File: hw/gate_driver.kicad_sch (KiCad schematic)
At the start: 15 parts, among them IC501 LMG1210RVRT

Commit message: v0.3.0rc (v1.0.0rc) sch complete
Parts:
- removed D501: 0.62V, footprints:stm_STPS1170AF, symbol Device:D_Schottky
- removed IC501: LMG1210RVRT, footprints:ti_LMG1210RVRT, symbol ti_LMG1210RVRT:LMG1210RVRT
- removed TP19: GND, TestPoint:TestPoint_Pad_1.0x1.0mm, symbol Connector:TestPoint
- removed TP8: 5V, TestPoint:TestPoint_Pad_1.0x1.0mm, symbol Connector:TestPoint
- added C503: 100n, Resistor_SMD:R_0402_1005Metric, symbol Device:C_Small
- added C504: 470n, Resistor_SMD:R_0402_1005Metric, symbol Device:C_Small
- added D501, D502: GRN, LED_SMD:LED_0402_1005Metric, symbol Device:LED_Small
- added D503, D504, D505: 0.55, footprints:stm_STPS1170AF, symbol Device:D_Schottky_Small
- added D506, D507: 5.1, Diode_SMD:D_SOD-123, symbol Device:D_Zener_Small
- added Q501: BSS127S, Package_TO_SOT_SMD:SOT-23, symbol Transistor_FET:BSS127S
- added R505, R506, R507, R508: 0, Resistor_SMD:R_0402_1005Metric, symbol Device:R_Small
- added R509: 1.5, Resistor_SMD:R_0402_1005Metric, symbol Device:R_Small
- added SB501, SB502: Jumper, Jumper:SolderJumper-2_P1.3mm_Open_TrianglePad1.0x1.5mm, symbol Jumper:SolderJumper_2_Bridged
- added TP502: SWH+, TestPoint:TestPoint_Keystone_5000-5004_Miniature, symbol Connector:TestPoint
- added TP506: SWLO, TestPoint:TestPoint_Keystone_5000-5004_Miniature, symbol Connector:TestPoint
- added TP507: GND, TestPoint:TestPoint_Keystone_5000-5004_Miniature, symbol Connector:TestPoint
- added TP508: PWM_CONV, TestPoint:TestPoint_Keystone_5000-5004_Miniature, symbol Connector:TestPoint
- added TP509: GNDPWR, TestPoint:TestPoint_Keystone_5000-5004_Miniature, symbol Connector:TestPoint
- added TP510: EN_CONV, TestPoint:TestPoint_Keystone_5000-5004_Miniature, symbol Connector:TestPoint
- added U501: ADUM4221-1ARIZ, footprints:ad_ADUM5221_1ARIZ, symbol ad_ADUM5221_1ARIZ:ADUM4221-1ARIZ
- C501: value 10uF -> 1u; footprint Capacitor_SMD:C_0603_1608Metric -> Resistor_SMD:R_0402_1005Metric; Cost 0.0234 -> 0.0068; Distributor JLCPCB -> LCSC; LCSC Part # C96446 -> C307454; Manufacturer Samsung Electro-Mechanics -> Samsung Electromechanics; Notes (none) -> Bulk capacitance.; P/N CL10A106MA8NRNC -> CL05X105KA5NQNC
- C502: value 100nF -> 1u; footprint Capacitor_SMD:C_0402_1005Metric -> Resistor_SMD:R_0402_1005Metric; Cost 0.0063 -> 0.0068; Distributor JLCPCB -> LCSC; LCSC Part # CL05B104KB54PNC -> C307454; Manufacturer Samsung Electro-Mechanics -> Samsung Electromechanics; Notes Rated for 50V. -> Bulk capacitance.; P/N CL05B104KB54PNC -> CL05X105KA5NQNC
- C505: value 1uF -> 10u; footprint Capacitor_SMD:C_0402_1005Metric -> Resistor_SMD:R_0805_2012Metric; Cost 0.0039 -> 0.34; Distributor JLCPCB -> Mouser; LCSC Part # C52923 -> (none); Manufacturer Samsung Electro-Mechanics -> Murata; Notes (none) -> Shall be C0G or X7R, low ESR.; P/N CL05A105KA5NQNC -> GRT21BC71E106KE13L
- R501: value 20k -> 330; Distributor JLCPCB -> LCSC; LCSC Part # C25765 -> C25105; Manufacturer Uniroyal Elec -> Uniroyal; P/N 0402WGF2002TCE -> 0402WGF330JTCE
- R502: value 1.8 -> 1k; Cost 0.0009 -> 0.0005; Distributor JLCPCB -> LCSC; LCSC Part # C423254 -> C11702; Manufacturer Uniroyal Elec -> Uniroyal; P/N 0402WGF118KTCE -> 0402WGF1001TCE
- R503: value 20k -> 1k; Distributor JLCPCB -> LCSC; LCSC Part # C25765 -> C11702; Manufacturer Uniroyal Elec -> Uniroyal; P/N 0402WGF2002TCE -> 0402WGF1001TCE
- R504: value 1.8 -> 4k; footprint Resistor_SMD:R_0402_1005Metric -> Resistor_SMD:R_0805_2012Metric; Cost 0.0009 -> 0.59; Distributor JLCPCB -> Mouser; LCSC Part # C423254 -> (none); Manufacturer Uniroyal Elec -> Vishay; P/N 0402WGF118KTCE -> CRCW08054K00FKTA
- TP501: value SW1_TP -> VBUS_DRIVE_3V3; footprint TestPoint:TestPoint_Keystone_5005-5009_Compact -> TestPoint:TestPoint_Keystone_5000-5004_Miniature; Cost (none) -> 0.31; Distributor (none) -> Mouser; Manufacturer (none) -> Keystone Electronics; Notes (none) -> Red (Logic Power); P/N (none) -> 5000
- TP503: value SW2_TP -> V_SW; footprint TestPoint:TestPoint_Keystone_5005-5009_Compact -> TestPoint:TestPoint_Keystone_5000-5004_Miniature; Cost (none) -> 0.36; Distributor (none) -> Mouser; Manufacturer (none) -> Keystone Electronics; Notes (none) -> Blue (Power Path Measurement); P/N (none) -> 5117
- TP504: value PWMEN_TP -> VBUS_DRIVE_5V0; footprint TestPoint:TestPoint_Pad_1.0x1.0mm -> TestPoint:TestPoint_Keystone_5000-5004_Miniature; Cost (none) -> 0.31; Distributor (none) -> Mouser; Manufacturer (none) -> Keystone Electronics; Notes (none) -> Red (Logic Power); P/N (none) -> 5000
- TP505: value PWM_TP -> SWHO; footprint TestPoint:TestPoint_Pad_1.0x1.0mm -> TestPoint:TestPoint_Keystone_5000-5004_Miniature; Cost (none) -> 0.36; Distributor (none) -> Mouser; Manufacturer (none) -> Keystone Electronics; Notes (none) -> Blue (Power Path Measurement); P/N (none) -> 5117
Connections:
- net EN/HI is gone; now on net VBUS_DRIVE_5V0: TP504.1
- net PWM/LI is gone; now on net SWHO: TP505.1
- net GND: now also R504.2, C503.2, D501.1 (K), Q501.2 (S), TP507.1, U501.4 (GND1); no longer C502.2, R501.2, R503.1
- net SWHO: now also D507.1 (K), R506.2, R508.2; no longer R504.1, TP503.1
- net SWLO: now also D506.1 (K), R505.2, R507.2, TP506.1; no longer R502.1, TP501.1
- net V_{SW}: now also TP503.1, C504.2, D507.2 (A), U501.14 (GNDA); no longer C505.2
- net at R502.2: now also D502.2 (A)
- net VBUS_DRIVE_5V0: now reaches C505.1
- net VBUS_DRIVE_5V0: now also C502.1, R502.1, R509.1, SB502.2 (B), U501.11 (VDDB)
- net VBUS_DRIVE_3V3: now reaches R501.1
- net VBUS_DRIVE_3V3: now also C501.1, R503.1, TP501.1, C503.1, SB501.2 (B), U501.3 (VDD1), U501.8 (VDD1)
- net at R503.2: now also Q501.3 (D), U501.5 (DISABLE)
- removed net +5V: C501.1, C502.1
- new net: D503.1 (K), R505.1, U501.10 (VOB)
- new net: D503.2 (A), R507.1
- new net: D504.1 (K), R506.1, U501.15 (VOA)
- new net: D505.2 (A), R509.2
- new net: D501.2 (A), R501.2
- new net: D504.2 (A), R508.1
- new net: R504.1, U501.6 (DT)
- new net +3.3VP: SB501.1 (A)
- new net +5VP: SB502.1 (A)
- new net EN_CONV: Q501.1 (G), TP510.1
- new net GNDPWR: C502.2, C505.2, D502.1 (K), D506.2 (A), TP509.1, U501.9 (GNDB)
- new net PWM_CONV: TP508.1, U501.1 (PWM)
- new net SWH+: C504.1, D505.1 (K), TP502.1, U501.16 (VDDA)
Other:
- note added: "IB"

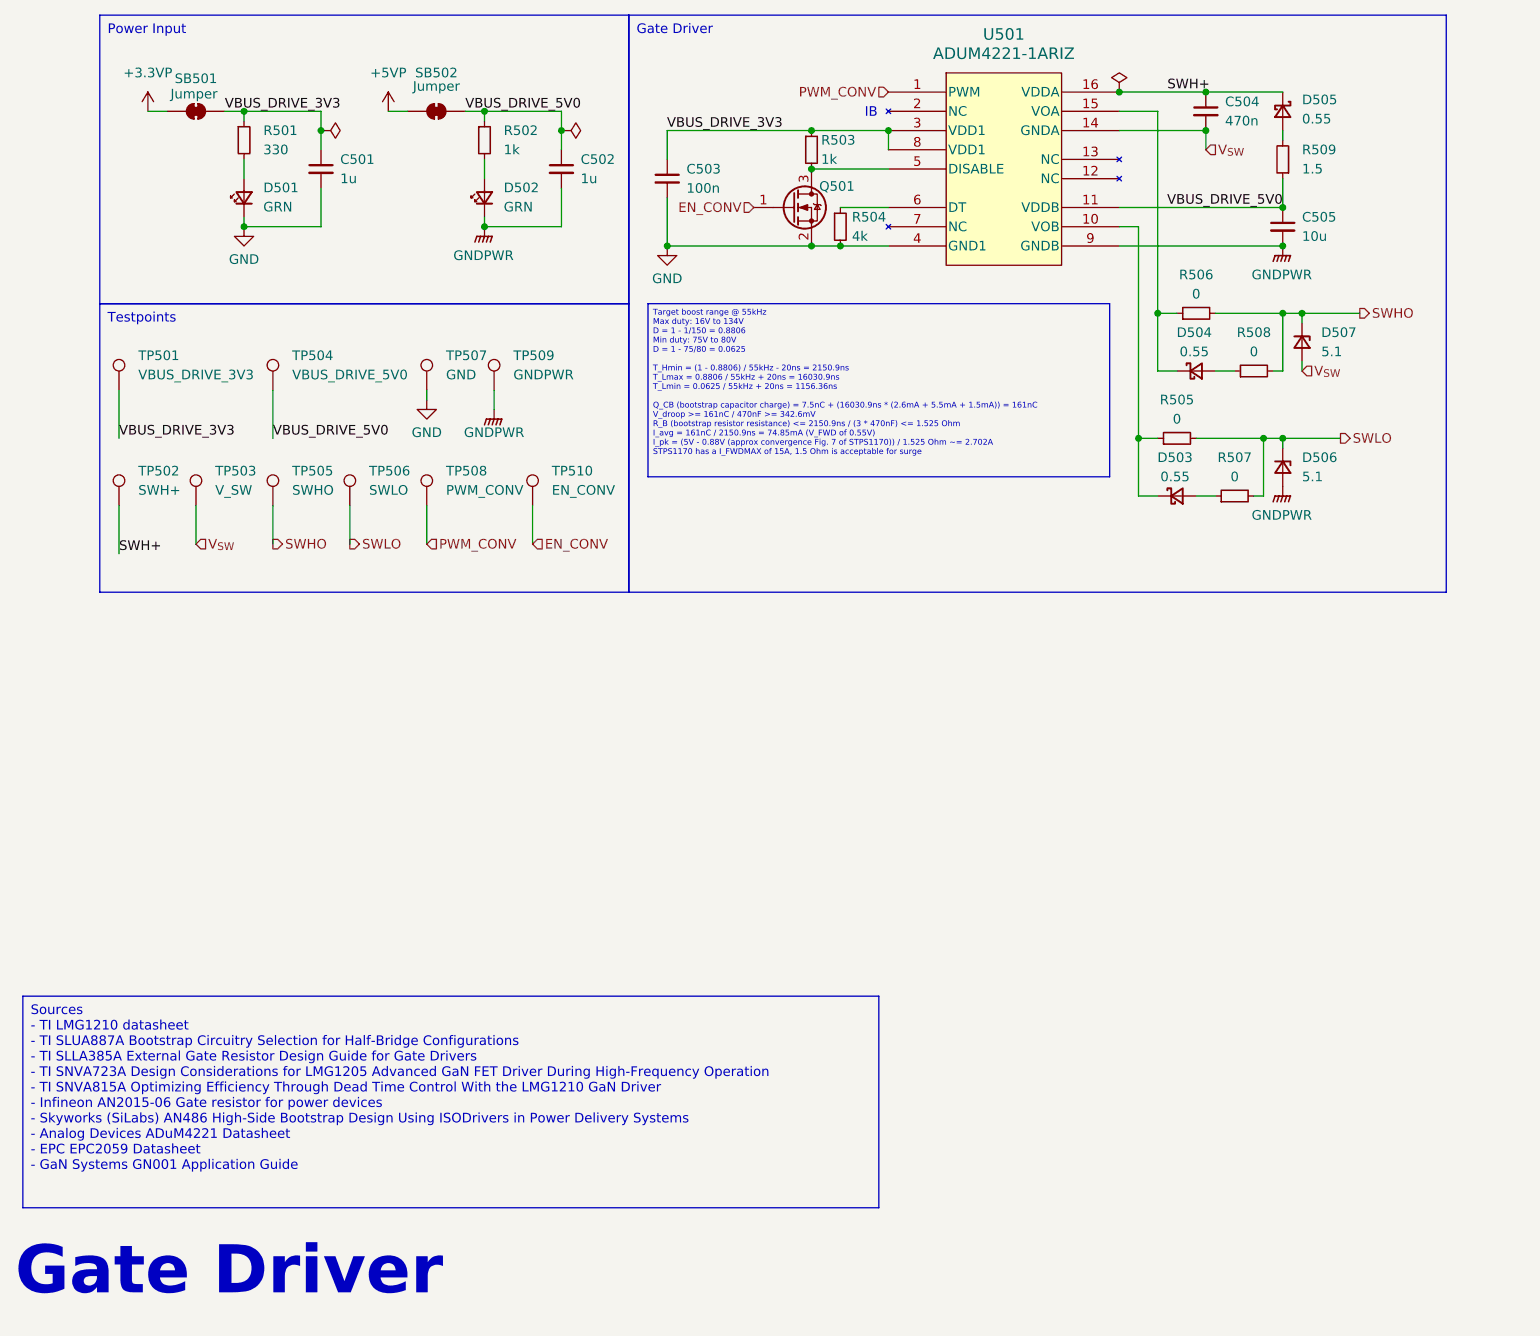
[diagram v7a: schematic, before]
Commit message: HW sch changes, further layout progression
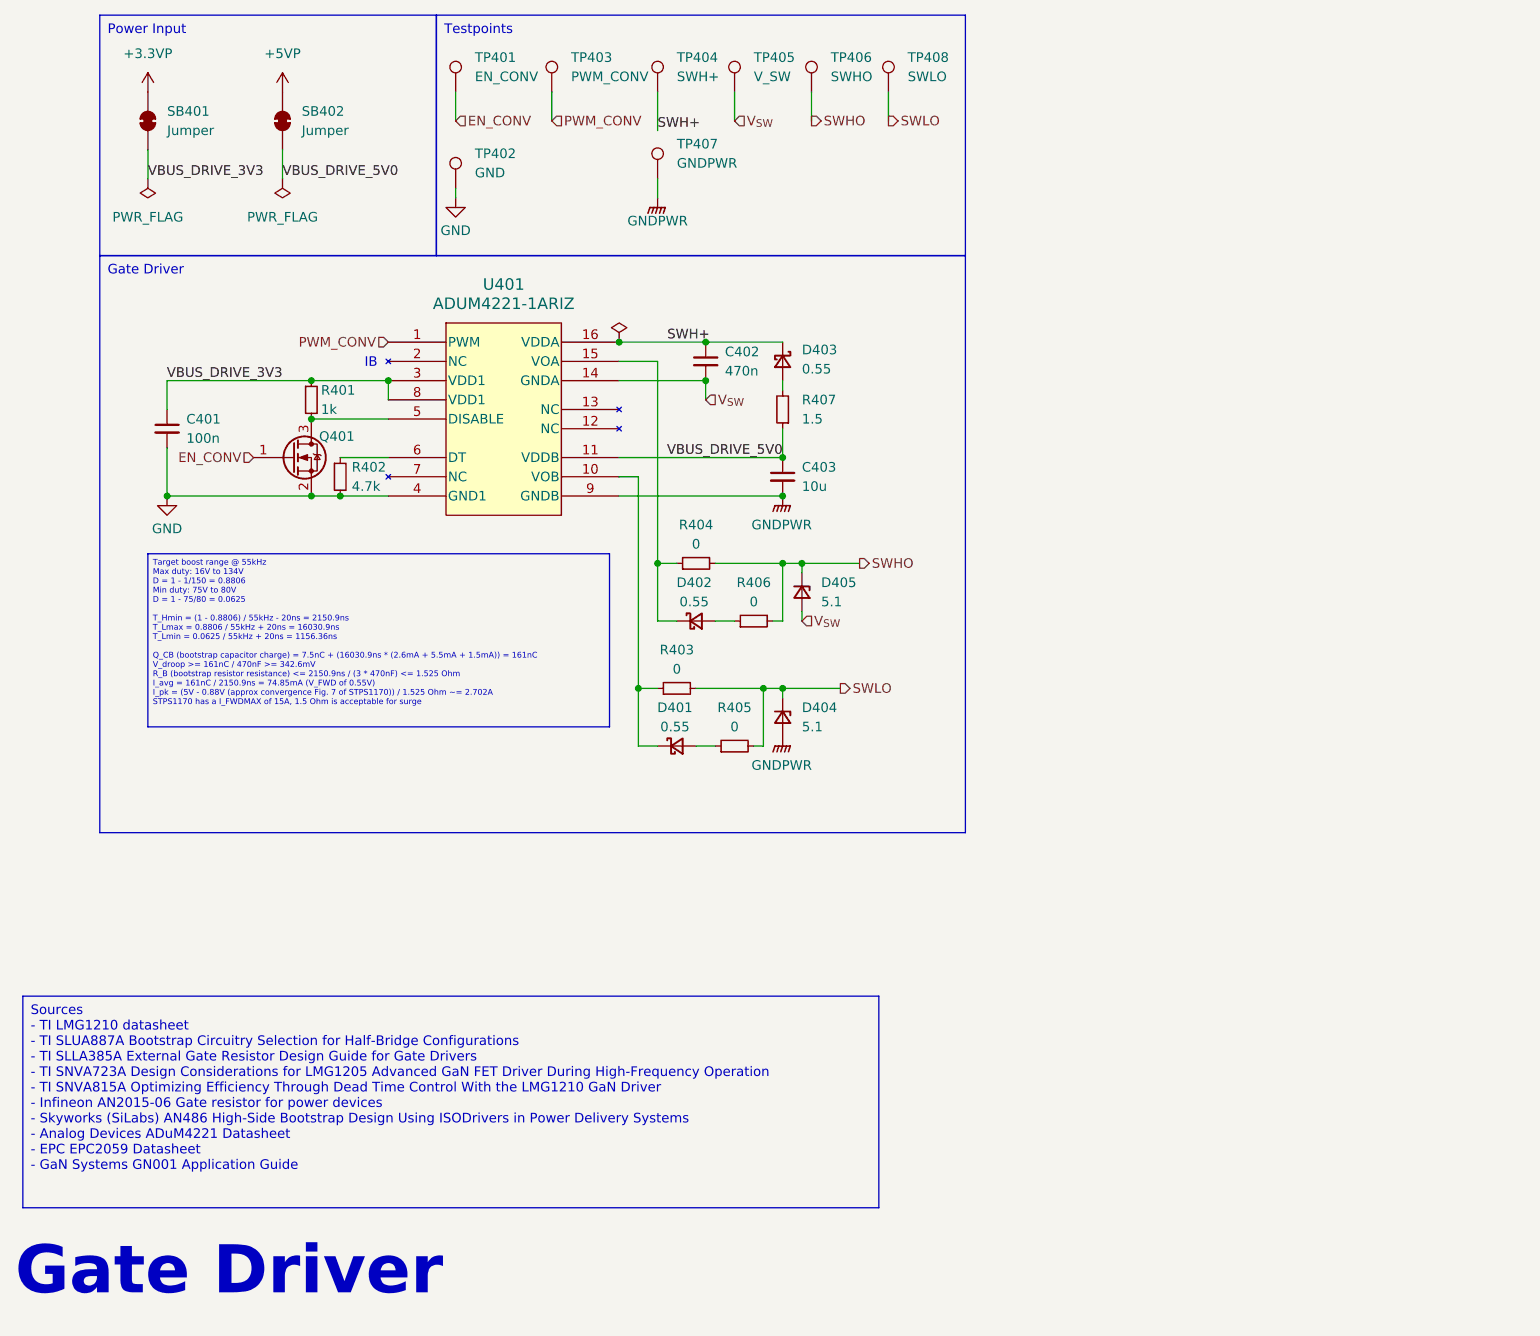
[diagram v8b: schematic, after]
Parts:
- removed C501, C502: 1u, Resistor_SMD:R_0402_1005Metric, symbol Device:C_Small
- removed D501, D502: GRN, LED_SMD:LED_0402_1005Metric, symbol Device:LED_Small
- removed R501: 330, Resistor_SMD:R_0402_1005Metric, symbol Device:R_Small
- removed R502: 1k, Resistor_SMD:R_0402_1005Metric, symbol Device:R_Small
- removed SB501, SB502: Jumper, Jumper:SolderJumper-2_P1.3mm_Open_TrianglePad1.0x1.5mm, symbol Jumper:SolderJumper_2_Bridged
- removed TP501: VBUS_DRIVE_3V3, TestPoint:TestPoint_Keystone_5000-5004_Miniature, symbol Connector:TestPoint
- removed TP504: VBUS_DRIVE_5V0, TestPoint:TestPoint_Keystone_5000-5004_Miniature, symbol Connector:TestPoint
- added SB401, SB402: Jumper, Jumper:SolderJumper-2_P1.3mm_Open_TrianglePad1.0x1.5mm, symbol Jumper:SolderJumper_2_Bridged
- R402: renamed from R504; value 4k -> 4.7k; footprint Resistor_SMD:R_0805_2012Metric -> Resistor_SMD:R_0402_1005Metric; Cost 0.59 -> 0.0005; Distributor Mouser -> LCSC; LCSC Part # (none) -> C25900; Manufacturer Vishay -> Uniroyal; Notes (none) -> DT ~= 4.7*5 ns (23.5ns); P/N CRCW08054K00FKTA -> 0402WGF4701TCE
- TP401: renamed from TP510; footprint TestPoint:TestPoint_Keystone_5000-5004_Miniature -> TestPoint:TestPoint_Pad_D1.5mm; Cost 0.38 -> (none); Distributor Mouser -> (none); Manufacturer Keystone Electronics -> (none); Notes White (Digital Signal) -> (none); P/N 5002 -> (none)
- TP402: renamed from TP507; footprint TestPoint:TestPoint_Keystone_5000-5004_Miniature -> TestPoint:TestPoint_Pad_D1.5mm; Cost 0.37 -> (none); Distributor Mouser -> (none); Manufacturer Keystone Electronics -> (none); Notes Black (Logic Ground) -> (none); P/N 5001 -> (none)
- TP403: renamed from TP508; footprint TestPoint:TestPoint_Keystone_5000-5004_Miniature -> TestPoint:TestPoint_Pad_D1.5mm; Cost 0.38 -> (none); Distributor Mouser -> (none); Manufacturer Keystone Electronics -> (none); Notes White (Digital Signal) -> (none); P/N 5002 -> (none)
- TP404: renamed from TP502; footprint TestPoint:TestPoint_Keystone_5000-5004_Miniature -> TestPoint:TestPoint_Pad_D1.5mm; Cost 0.36 -> (none); Distributor Mouser -> (none); Manufacturer Keystone Electronics -> (none); Notes Blue (Power Path Measurement) -> (none); P/N 5117 -> (none)
- TP405: renamed from TP503; footprint TestPoint:TestPoint_Keystone_5000-5004_Miniature -> TestPoint:TestPoint_Pad_D1.5mm; Cost 0.36 -> (none); Distributor Mouser -> (none); Manufacturer Keystone Electronics -> (none); Notes Blue (Power Path Measurement) -> (none); P/N 5117 -> (none)
- TP406: renamed from TP505; footprint TestPoint:TestPoint_Keystone_5000-5004_Miniature -> TestPoint:TestPoint_Pad_D1.5mm; Cost 0.36 -> (none); Distributor Mouser -> (none); Manufacturer Keystone Electronics -> (none); Notes Blue (Power Path Measurement) -> (none); P/N 5117 -> (none)
- TP407: renamed from TP509; footprint TestPoint:TestPoint_Keystone_5000-5004_Miniature -> TestPoint:TestPoint_Pad_D1.5mm; Cost 0.37 -> (none); Distributor Mouser -> (none); Manufacturer Keystone Electronics -> (none); Notes Brown (Power Path Ground) -> (none); P/N 5115 -> (none)
- TP408: renamed from TP506; footprint TestPoint:TestPoint_Keystone_5000-5004_Miniature -> TestPoint:TestPoint_Pad_D1.5mm; Cost 0.36 -> (none); Distributor Mouser -> (none); Manufacturer Keystone Electronics -> (none); Notes Blue (Power Path Measurement) -> (none); P/N 5117 -> (none)
- renumbered C503 to C401, C504 to C402, C505 to C403, D503 to D401, D504 to D402, D505 to D403, D506 to D404, D507 to D405, Q501 to Q401, R503 to R401, R505 to R403, R506 to R404, R507 to R405, R508 to R406, R509 to R407, U501 to U401
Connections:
- net +3.3VP: now also SB401.2 (B)
- net +5VP: now also SB402.2 (B)
- net VBUS_DRIVE_3V3: now also SB401.1 (A)
- net VBUS_DRIVE_5V0: now also SB402.1 (A)
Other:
- moved on the sheet: C401, C402, C403, D401, D402, D403, D404, D405, Q401, R401, R402, R403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
